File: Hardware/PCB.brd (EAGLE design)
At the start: 160 x 100 mm, 105 parts, among them IC1 BQ25180YBGR, IC2 DRV2605YZFR, IC3 BMA421, IC9 RT6160AWSC, J1 503480-2400, J2 TC2030-IDC, J4 KH-TYPE-C-16P, Q1 20V/4.2A/52mΩ/1.4W, Q3 SI1308EDL-T1-GE3, U1 NRF52840 _QF, U3 MAX17048G+T10, X1 32MHz, X2 32.768KHz

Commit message: Remade Schematic + PCB
Remade schematic and started on PCB a bit
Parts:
- removed ANT1: 2450AT18B100E, InkTime_v5:2450AT18B100E_ANTC3216X140N
- removed D3: USBLC6-2SC6Y, InkTime_v5:ESP32_C6_LIBRARY_3_SOT95P280X145-6N
- removed IC3: BMA421, InkTime_v5:BMA423_BMA423
- removed IC9: RT6160AWSC, InkTime_v5:RT6160AWSC_BGA15C40P3X5_140X230X60
- removed J4: KH-TYPE-C-16P, InkTime_v5:KH-TYPE-C-16P_KINGHELM_KH-TYPE-C-16P
- removed L7: FTC252012SR47MBCA, InkTime_v5:MLP2016SR47MT0S1_INDC2016X100N
- removed U3: MAX17048G+T10, InkTime_v5:ESP32_C6_LIBRARY_SON50P200X200X80-9N
- added ANT2: 2450AT18B100E_2450AT18B100E, InkTime_v5:2450AT18B100E_ANTC3216X140N
- added D1: ESP32_C6_LIBRARY_3_USBLC6-2SC6Y, InkTime_v5:ESP32_C6_LIBRARY_3_SOT95P280X145-6N
- added IC4: BMA423_BMA423, InkTime_v5:BMA423_BMA423
- added IC5: DRV2605YZFR_DRV2605YZFR, InkTime_v5:DRV2605YZFR_BGA9C50P3X3_144X144X62
- added J3: 503480-2400_503480-2400, InkTime_v5:503480-2400_5034802400
- added L4: 15nH, InkTime_v5:MLP2016SR47MT0S1_INDC2016X100N
- added U$1: NORDIC_NRF_4_NRF52840_QF, InkTime_v5:NORDIC_NRF_4_AQFN50P700X700X85_HS-74N
- IC1: value BQ25180YBGR -> RT6160AWSC_RT6160AWSC; device InkTime_v5:BQ25180YBGR_BGA8C40P2X4_100X155X50 -> InkTime_v5:RT6160AWSC_BGA15C40P3X5_140X230X60
- IC2: value DRV2605YZFR -> BQ25180YBGR_BQ25180YBGR; device InkTime_v5:DRV2605YZFR_BGA9C50P3X3_144X144X62 -> InkTime_v5:BQ25180YBGR_BGA8C40P2X4_100X155X50
- J1: value 503480-2400 -> TC2030-IDC_TC2030-IDC; device InkTime_v5:503480-2400_5034802400 -> InkTime_v5:TC2030-IDC_TC2030IDC
- J2: value TC2030-IDC -> KH-TYPE-C-16P_KH-TYPE-C-16P; device InkTime_v5:TC2030-IDC_TC2030IDC -> InkTime_v5:KH-TYPE-C-16P_KINGHELM_KH-TYPE-C-16P
- L1: value 3.9nH -> MLP2016SR47MT0S1_FTC252012SR47MBCA
- L2: value 10uH -> 3.9nH
- L3: value 15nH -> 10uH
- U1: value NRF52840 _QF -> ESP32_C6_LIBRARY_MAX17048G+T10; device InkTime_v5:NORDIC_NRF_4_AQFN50P700X700X85_HS-74N -> InkTime_v5:ESP32_C6_LIBRARY_SON50P200X200X80-9N
- moved R5 121.9 mm to (-135.9, 168.9)
- moved J1 110.3 mm to (-6.35, 101.6)
- moved J2 108.6 mm to (-119.4, 87.6)
- moved U1 90.5 mm to (-45.7, 141.0)
- moved C1-EP-DR 81.3 mm to (-116.8, 141.0)
- moved C2-EP-DR 81.3 mm to (-127.0, 141.0)
- moved EPD_C5 81.3 mm to (-135.9, 141.0)
- moved C11 78.8 mm to (-130.8, 147.3)
- moved C7 78.8 mm to (-111.8, 147.3)
- moved C8 78.8 mm to (-118.1, 147.3)
- moved C5 78.8 mm to (-105.4, 147.3)
- moved C9 78.8 mm to (-124.5, 147.3)
- moved IC2 73.1 mm to (-88.9, 165.1)
- moved EPD_C9 72.4 mm to (-92.7, 147.3)
- moved IC1 70.3 mm to (-57.1, 165.1)
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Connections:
- new net N$24: J3.17
- new net N$3: C7.1, U$1.P$AD14
- new net N$34: J2.A12_B1, J2.A1_B12
- new net N$35: J2.B6
- new net N$36: J2.B7
- new net N$7: IC5.B1
- net 3V3/1.7D: now also IC5.C2; no longer IC2.C2
- net 3V3/2.4A: now also IC1.E2, IC1.E3, IC4.10, IC4.3, IC4.7, J1.1, U$1.P$AD23, U$1.P$W1, U$1.P$Y2; no longer C7.1, IC3.10, IC3.3, IC3.7, IC9.E2, IC9.E3, J2.1, U1.P$AD14, U1.P$AD23, U1.P$W1, U1.P$Y2
- net ALERT/1.6C: now also U1.5; no longer U3.5
- net ALERT/2.5C: now also U$1.P$J24; no longer U1.P$J24
- net D+/1.5D: now also D1.4; no longer D3.4
- net D+/2.7D: now also U$1.P$AD6; no longer U1.P$AD6
- net D-/1.5D: now also D1.6; no longer D3.6
- net D-/2.7D: now also U$1.P$AD4; no longer U1.P$AD4
- net DEC1: now also U$1.P$C1; no longer U1.P$C1
- net DEC4_6: now also L4.2, U$1.P$B5, U$1.P$E24; no longer L3.2, U1.P$B5, U1.P$E24
- net DN: now also D1.1, J2.A7; no longer D3.1, J4.A7, J4.B7
- net DP: now also D1.3, J2.A6; no longer D3.3, J4.A6, J4.B6
- net EPD_3V3: now also J3.15, J3.16; no longer J1.15, J1.16
- net EPD_BUSY/1.5D: now also J3.9; no longer J1.9
- net EPD_BUSY/2.2D: now also U$1.P$AD12; no longer U1.P$AD12
- net EPD_CS/1.4C: now also J3.12; no longer J1.12
- net EPD_CS/2.2D: now also U$1.P$K2; no longer U1.P$K2
- net EPD_DC/1.5D: now also J3.11; no longer J1.11
- net EPD_DC/2.2D: now also U$1.P$AD10; no longer U1.P$AD10
- net EPD_RST/1.5D: now also J3.10; no longer J1.10
- net EPD_RST/2.2D: now also U$1.P$AC11; no longer U1.P$AC11
- net GDR: now also J3.2; no longer J1.2
- net GND: now also D1.2, IC1.B1, IC1.C1, IC1.C2, IC1.C3, IC2.D2, IC4.8, IC4.9, IC5.B3, J1.3, J1.5, J2.SH1, J2.SH2, J2.SH3, J2.SH4, J3.8, J3.MP1, J3.MP2, U$1.P$74, U$1.P$75, U$1.P$76, U$1.P$77, U$1.P$78, U$1.P$79, U$1.P$80, U$1.P$81, U$1.P$82, U$1.P$83, U$1.P$84, U$1.P$85, U$1.P$86, U$1.P$87, U$1.P$88, U$1.P$89, U$1.P$90, U$1.P$B7, U$1.P$F23, U1.1, U1.4, U1.6, U1.9; no longer D3.2, IC1.D2, IC2.B1, IC2.B3, IC3.8, IC3.9, IC9.B1, IC9.C1, IC9.C2, IC9.C3, J1.17, J1.8, J1.MP1, J1.MP2, J2.3, J2.5, J4.A12_B1, J4.A1_B12, J4.SH1, J4.SH2, J4.SH3, J4.SH4, U1.P$74, U1.P$75, U1.P$76, U1.P$77, U1.P$78, U1.P$79, U1.P$80, U1.P$81, U1.P$82, U1.P$83, U1.P$84, U1.P$85, U1.P$86, U1.P$87, U1.P$88, U1.P$89, U1.P$90, U1.P$B7, U1.P$F23, U3.1, U3.4, U3.6, U3.9
- net HAPTIC_EN/1.4C: now also IC5.A1; no longer IC2.A1
- net HAPTIC_EN/2.6A: now also U$1.P$U1; no longer U1.P$U1
- net IMU_INT1: now also IC4.5, U$1.P$N1; no longer IC3.5, U1.P$N1
- net IMU_INT2: now also IC4.6, U$1.P$P2; no longer IC3.6, U1.P$P2
- net LX1: now also IC1.B2, IC1.B3, L1.1; no longer IC9.B2, IC9.B3, L7.1
- net LX2: now also IC1.D2, IC1.D3, L1.2; no longer IC9.D2, IC9.D3, L7.2
- net MOSI/1.5B: now also J3.14; no longer J1.14
- net MOSI/2.2D: now also U$1.P$B13; no longer U1.P$B13
- net N$1: now also U$1.P$D23; no longer U1.P$D23
- net N$10: now also L3.1, U$1.P$B3; no longer L2.1, U1.P$B3
- net N$11: now also U$1.P$AD18; no longer U1.P$AD18
- net N$12: now also L3.2, L4.1; no longer L2.2, L3.1
- net N$13: now also U$1.P$A18; no longer U1.P$A18
- net N$14: now also U$1.P$A22; no longer U1.P$A22
- net N$15: now also IC4.1; no longer IC3.1
- net N$16: now also IC1.D1; no longer IC9.D1
- net N$17: now also IC1.E1; no longer IC9.E1
- net N$19: now also IC2.D1; no longer IC1.D1
- net N$2: now also L2.1, U$1.P$H23; no longer L1.1, U1.P$H23
- net N$23: now also J3.4; no longer J1.4
- net N$25: now also J3.5; no longer J1.5
- net N$26: now also J3.18; no longer J1.18
- net N$27: now also J3.19; no longer J1.19
- net N$28: now also J3.20; no longer J1.20
- net N$29: now also J3.22; no longer J1.22
- net N$30: now also J3.24; no longer J1.24
- net N$31: now also IC5.A2; no longer IC2.A2
- net N$32: now also J2.A5; no longer J4.A5
- net N$33: now also J2.B5; no longer J4.B5
- net N$4: now also U$1.P$B24; no longer U1.P$B24
- net N$5: now also U$1.P$A23; no longer U1.P$A23
- net N$6: now also U$1.P$AC5; no longer U1.P$AC5
- net N$8: now also U$1.P$N24; no longer U1.P$N24
- net N$9: now also U$1.P$B1; no longer U1.P$B1
- net OUT: now also IC5.C3; no longer IC2.C3
- net OUT+: now also IC5.A3; no longer IC2.A3
- net P0.00/XL1: now also U$1.P$D2; no longer U1.P$D2
- net P0.01/XL2: now also U$1.P$F2; no longer U1.P$F2
- net P0.04: now also U$1.P$J1; no longer U1.P$J1
- net P0.09: now also U$1.P$L24; no longer U1.P$L24
- net P0.26: now also U$1.P$G1; no longer U1.P$G1
- net P0.27: now also U$1.P$H2; no longer U1.P$H2
- net P0.28: now also U$1.P$B11; no longer U1.P$B11
- net P0.29: now also U$1.P$A10; no longer U1.P$A10
- net P0.30: now also U$1.P$B9; no longer U1.P$B9
- net P0.31: now also U$1.P$A8; no longer U1.P$A8
- net P1.01/2.4B: now also U$1.P$Y23; no longer U1.P$Y23
- net P1.02/2.8C: now also U$1.P$W24; no longer U1.P$W24
- net P1.03: now also U$1.P$V23; no longer U1.P$V23
- net P1.04: now also U$1.P$U24; no longer U1.P$U24
- net P1.05: now also U$1.P$T23; no longer U1.P$T23
- net P1.06: now also U$1.P$R24; no longer U1.P$R24
- net P1.07: now also U$1.P$P23; no longer U1.P$P23
- net P1.09: now also U$1.P$R1; no longer U1.P$R1
- net P1.10: now also U$1.P$A20; no longer U1.P$A20
- net P1.11: now also U$1.P$B19; no longer U1.P$B19
- net P1.12: now also U$1.P$B17; no longer U1.P$B17
- net P1.13: now also U$1.P$A16; no longer U1.P$A16
- net P1.14: now also U$1.P$B15; no longer U1.P$B15
- net P1.15: now also U$1.P$A14; no longer U1.P$A14
- net PMIC_INT: now also IC2.A1, U$1.P$T2; no longer IC1.A1, U1.P$T2
- net PO.13/2.6C: now also U$1.P$AD8; no longer U1.P$AD8
- net PO.14/2.7C: now also U$1.P$AC9; no longer U1.P$AC9
- net PO.19: now also U$1.P$AC15; no longer U1.P$AC15
- net PO.20: now also U$1.P$AD16; no longer U1.P$AD16
- net PO.21: now also U$1.P$AC17; no longer U1.P$AC17
- net PO.22: now also U$1.P$AC19; no longer U1.P$AC19
- net PO.24: now also U$1.P$AD20; no longer U1.P$AD20
- net PO.25: now also U$1.P$AC21; no longer U1.P$AC21
- net PREVGH: now also J3.21; no longer J1.21
- net PREVGL: now also J3.23; no longer J1.23
- net RESE: now also J3.3; no longer J1.3
- net RESET: now also J1.6, U$1.P$AC13; no longer J2.6, U1.P$AC13
- net RF: now also ANT2.1, L2.2; no longer ANT1.1, L1.2
- net SCK/1.5B: now also J3.13; no longer J1.13
- net SCK/2.2D: now also U$1.P$A12; no longer U1.P$A12
- net SCL/1.4C: now also IC5.C1; no longer IC2.C1
- net SCL/2.4C: now also IC2.B1, IC4.12, U$1.P$M2, U1.7; no longer IC1.B1, U1.P$M2, U3.7
- net SDA/1.4C: now also IC5.B2; no longer IC2.B2
- net SDA/2.4C: now also IC2.C1, IC4.2, U$1.P$L1, U1.8; no longer IC1.C1, IC3.2, U1.P$L1, U3.8
- net SWDCLK: now also J1.4, U$1.P$AA24; no longer J2.4, U1.P$AA24
- net SWDIO: now also J1.2, U$1.P$AC24; no longer J2.2, U1.P$AC24
- net SWO: now also U$1.P$AD22; no longer U1.P$AD22
- net VBAT/1.2A: now also U1.2, U1.3; no longer U3.2, U3.3
- net VBAT/2.5C: now also IC2.C2; no longer IC1.C2
- net VBUS/1.5D: now also D1.5, J2.A4_B9, J2.A9_B4; no longer D3.5, J4.A4_B9, J4.A9_B4
- net VBUS/2.6D: now also IC2.A2, U$1.P$AD2; no longer IC1.A2, U1.P$AD2
- net VREG: now also IC1.A1, IC1.A2, IC1.A3, IC2.B2; no longer IC1.B2, IC9.A1, IC9.A2, IC9.A3
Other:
- board size 160 x 100 mm -> 46 x 35 mm

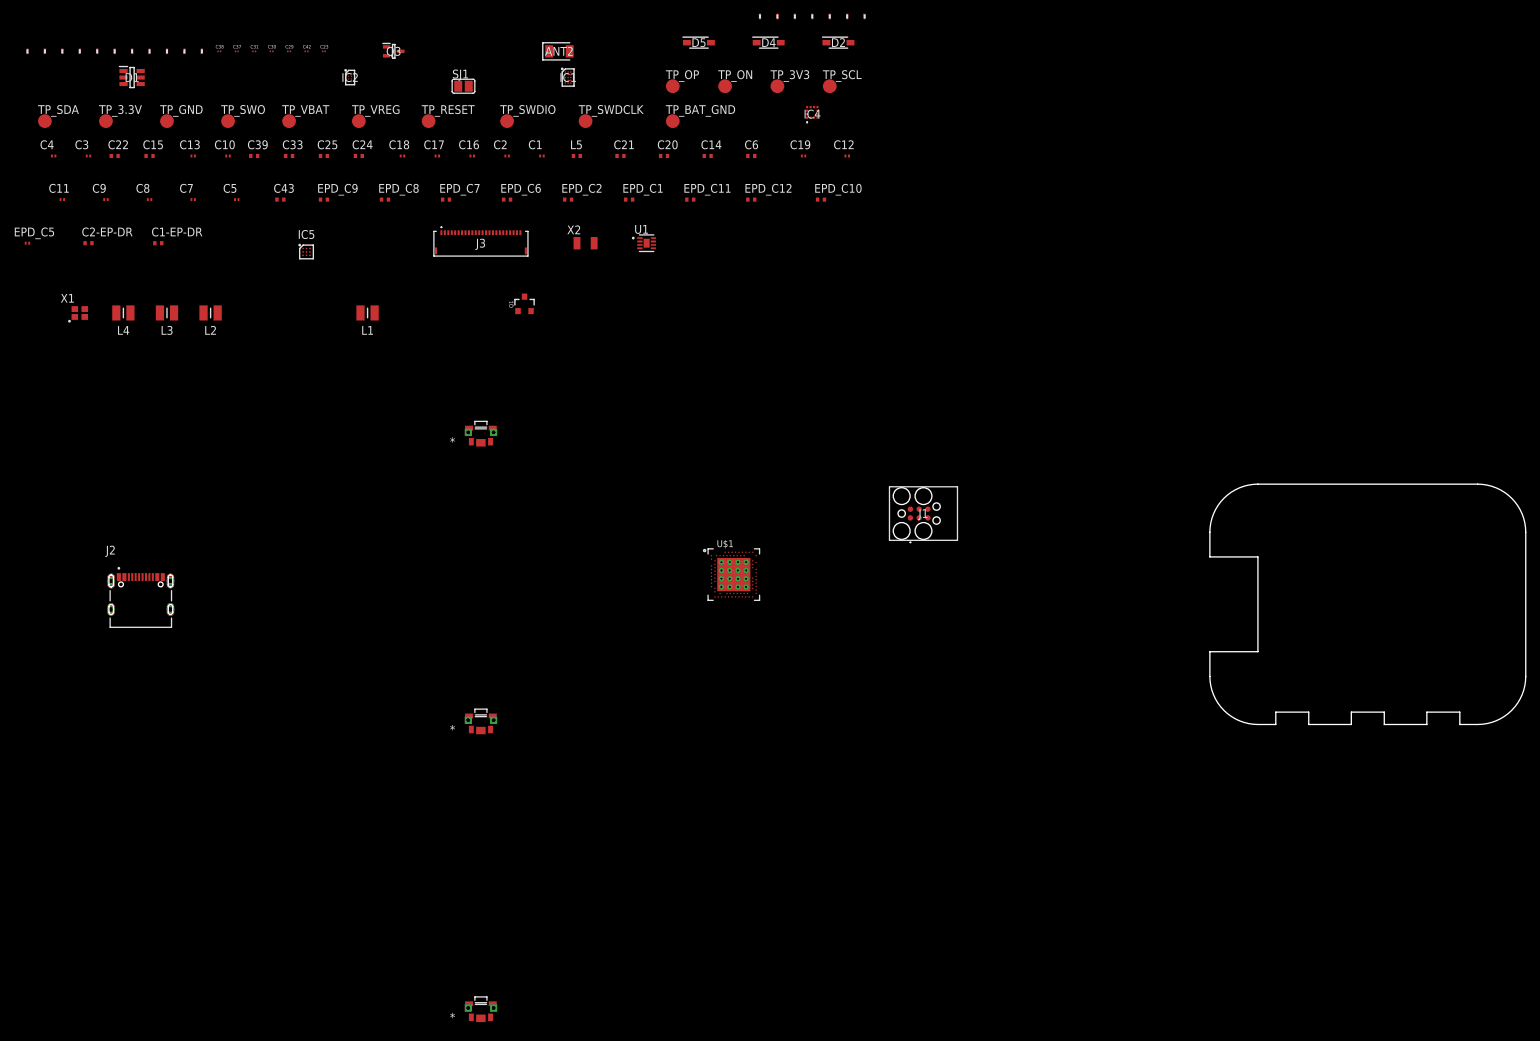
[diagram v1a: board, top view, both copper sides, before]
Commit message: Add some of the missing files and edits from PCB and Schematic
Added some images, edited out the schematic a bit added a 3D model for the USB. Also added Gerbers and BOM
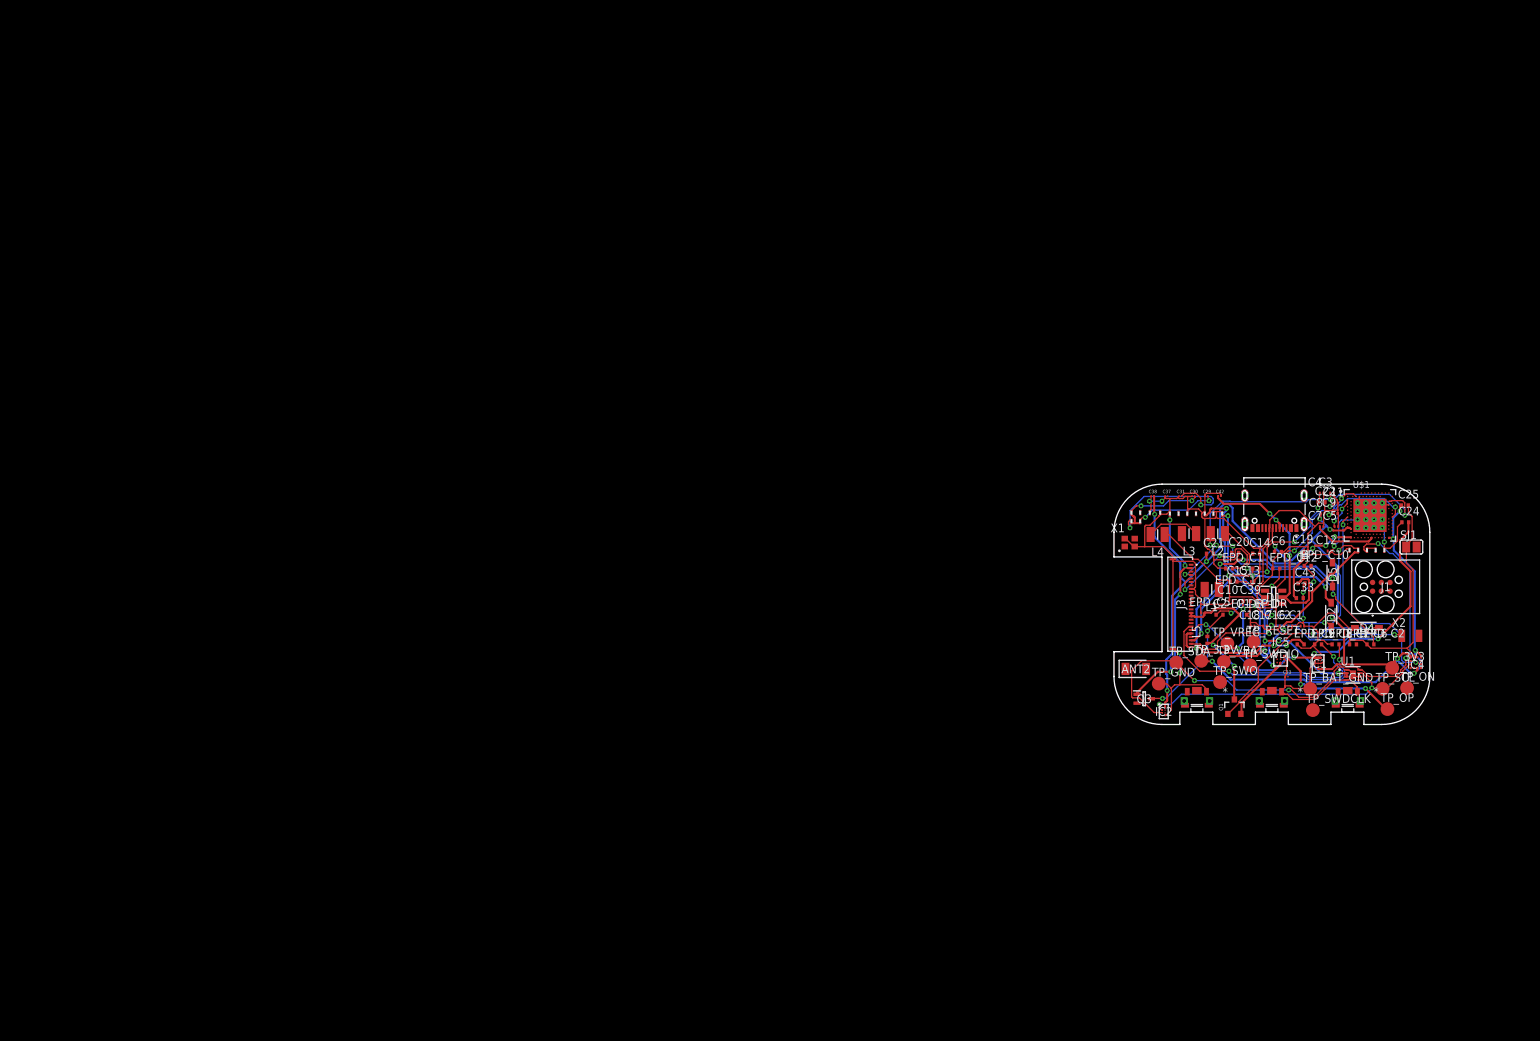
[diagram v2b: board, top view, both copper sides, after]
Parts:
- removed J2: KH-TYPE-C-16P_KH-TYPE-C-16P, InkTime_v5:KH-TYPE-C-16P_KINGHELM_KH-TYPE-C-16P
- added J4: KH-TYPE-C-16P_KH-TYPE-C-16PUSB, InkTime_v5:KH-TYPE-C-16P_KINGHELM_KH-TYPE-C-16P
- moved C4 191.1 mm to (52.6, 104.6)
- moved C11 190.7 mm to (54.7, 103.1)
- moved C3 187.6 mm to (54.1, 104.6)
- moved C9 184.8 mm to (54.6, 101.6)
- moved C22 182.9 mm to (52.6, 103.3)
- moved TP_SDA 182.7 mm to (31.4, 79.9)
- moved D1 182.7 mm to (45.6, 89.4)
- moved EPD_C5 179.5 mm to (35.3, 87.1)
- moved TP_3.3V 177.8 mm to (35.1, 80.1)
- moved C8 176.8 mm to (52.7, 101.6)
- moved R5 174.3 mm to (24.9, 101.7)
- moved C2-EP-DR 173.4 mm to (37.7, 86.9)
- moved R4 173.1 mm to (26.2, 101.7)
- moved R3 172.0 mm to (27.6, 101.7)
- moved C7 171.1 mm to (52.6, 99.7)
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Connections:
- net DN: now also J4.A5; no longer J2.A7
- net DP: now also J4.A7; no longer J2.A6
- net GND: now also J4.B6; no longer J2.SH1, J2.SH2, J2.SH3, J2.SH4
- net N$32: now also J4.A1_B12; no longer J2.A5
- net N$33: now also J4.A4_B9; no longer J2.B5
- net N$34: now also J4.A9_B4; no longer J2.A12_B1, J2.A1_B12
- net N$35: now also J4.A8; no longer J2.B6
- net N$36: now also J4.A6; no longer J2.B7
- net VBUS/1.5D: now also J4.B7; no longer J2.A4_B9, J2.A9_B4
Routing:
- net GND: track 0.00 -> 339.7 mm, vias 0 -> 9
- net 3V3/2.4A: track 0.00 -> 127.8 mm, vias 0 -> 11
- net SDA/2.4C: track 0.00 -> 79.3 mm, vias 0 -> 4
- net VBUS/2.6D: track 0.00 -> 74.0 mm, vias 0 -> 6
- net 3V3/1.7D: track 0.00 -> 62.2 mm, vias 0 -> 3
- net VREG: track 0.00 -> 54.2 mm, vias 0 -> 5
- net PREVGH: track 0.00 -> 53.7 mm, vias 0 -> 6
- net DEC4_6: track 0.00 -> 49.5 mm, vias 0 -> 2
- net VBAT/1.2A: track 0.00 -> 43.8 mm, vias 0 -> 5
- net SCL/2.4C: track 0.00 -> 43.5 mm, vias 0 -> 2
- net N$23: track 0.00 -> 38.3 mm, vias 0 -> 4
- net P1.01/1.6C: track 0.00 -> 36.6 mm, vias 0 -> 2
- net N$27: track 0.00 -> 34.9 mm, vias 0 -> 2
- net VBUS/1.5D: track 0.00 -> 33.5 mm, vias 0 -> 3
- net GDR: track 0.00 -> 32.1 mm, vias 0 -> 4
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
